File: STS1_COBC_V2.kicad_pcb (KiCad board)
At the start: 4 copper layers, 81 x 85 mm, 82 parts, among them IC2 STWD100PYW83F, IC3 STM32F411RET6TR, J1 Conn_Coaxial, J10 Conn_01x01_Male, J11 Conn_01x01_Male, J12 Conn_01x01_Male, J13 Conn_01x01_Male, J14 Conn_01x01_Male, J15 Conn_01x01_Male, J16 Conn_ARM_JTAG_SWD_10, J17 Conn_01x03_Male, J18 Conn_01x01_Male, J2 Conn_01x03_Male, J3 Conn_01x01_Male, J4 Conn_01x01_Female, J5 Conn_01x03_Male, J9 Conn_01x03_Male, U1 coordinate_system, U3 MCP1725-3302E_MC, Y1 Crystal_GND24

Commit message: more work done
All parts besides RF added
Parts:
- removed D3, D4, D5: LED, LED_SMD:LED_0805_2012Metric
- removed J10, J11, J14, J15, J3: Conn_01x01_Male, Connector_PinHeader_2.54mm:PinHeader_1x01_P2.54mm_Vertical
- removed J4: Conn_01x01_Female, Connector_PinHeader_2.54mm:PinHeader_1x01_P2.54mm_Vertical
- removed J9: Conn_01x03_Male, STS1library:PinHeader_1x03_P2.54mm_Vertical_umdieEcke
- removed R4, R6, R7: 300, Resistor_SMD:R_0805_2012Metric
- removed TP1, TP10, TP11, TP12, TP13, TP14, TP15, TP2, TP3, TP7, TP8, TP9: TestPoint, STS1library:STS1_Testpoint
- added 5V_RF: TestPoint, STS1library:STS1_Testpoint, F.Cu at (180.4, 57.4)
- added C36: 100uF, Capacitor_Tantalum_SMD:CP_EIA-7343-43_Kemet-X, F.Cu at (127.2, 78.8)
- added C37: 22uF, Capacitor_SMD:C_1206_3216Metric, F.Cu at (128.3, 73.1)
- added C38: 100nF, Capacitor_SMD:C_0603_1608Metric, F.Cu at (130.4, 75.8)
- added C39: 1uF, Capacitor_SMD:C_0805_2012Metric, F.Cu at (125.1, 70.3)
- added C40: 1uF, Capacitor_SMD:C_0805_2012Metric, F.Cu at (135.4, 79.5)
- added C41: 22nF, Capacitor_SMD:C_0603_1608Metric, F.Cu at (133.4, 79.3)
- added C42: 100nF, Capacitor_SMD:C_0603_1608Metric, F.Cu at (132.2, 72.7)
- added C43: 100nF, Capacitor_SMD:C_0603_1608Metric, F.Cu at (135.2, 72.7)
- added C44: 100nF, Capacitor_SMD:C_0603_1608Metric, F.Cu at (136.8, 76.2)
- added C45: 10uF, Capacitor_SMD:C_0805_2012Metric, F.Cu at (138.6, 76.5)
- added C46: 10uF, Capacitor_SMD:C_0805_2012Metric, F.Cu at (138.5, 73.7)
- added C47: 100uF, Capacitor_Tantalum_SMD:CP_EIA-7343-43_Kemet-X, F.Cu at (142.0, 79.2)
- added D10: BZY55C12 RYG, Diode_SMD:D_0805_2012Metric, F.Cu at (127.9, 84.2)
- added D11: AQ1003-01LTG, Diode_SMD:D_SOD-523, F.Cu at (140.9, 73.4)
- added D9: UCLAMP0871P.TNT, STS_Package_DFN_QFN:SGP1610N2, F.Cu at (124.0, 75.5)
- added EDU_EN: TestPoint, STS1library:STS1_Testpoint, F.Cu at (169.7, 118.4)
- added FLASH_CLK: Conn_01x01_Male, Connector_PinHeader_2.54mm:PinHeader_1x01_P2.54mm_Vertical, F.Cu at (126.2, 107.9)
- added FLASH_MISO: Conn_01x01_Male, Connector_PinHeader_2.54mm:PinHeader_1x01_P2.54mm_Vertical, F.Cu at (130.1, 112.2)
- added FLASH_MOSI: Conn_01x01_Male, Connector_PinHeader_2.54mm:PinHeader_1x01_P2.54mm_Vertical, F.Cu at (126.2, 112.2)
- added FLASH_VDD: TestPoint, STS1library:STS1_Testpoint, F.Cu at (145.3, 108.0)
- added FRAM_CLK: Conn_01x01_Male, Connector_PinHeader_2.54mm:PinHeader_1x01_P2.54mm_Vertical, F.Cu at (130.1, 99.2)
- added FRAM_CS: TestPoint, STS1library:STS1_Testpoint, F.Cu at (132.8, 109.4)
- added FRAM_MISO: Conn_01x01_Male, Connector_PinHeader_2.54mm:PinHeader_1x01_P2.54mm_Vertical, F.Cu at (130.1, 103.6)
- added FRAM_MOSI: Conn_01x01_Male, Connector_PinHeader_2.54mm:PinHeader_1x01_P2.54mm_Vertical, F.Cu at (130.1, 107.9)
- added FRAM_VDD: TestPoint, STS1library:STS1_Testpoint, F.Cu at (144.3, 100.1)
- added L2: 4.7uH, Inductor_SMD:L_12x12mm_H6mm, F.Cu at (133.8, 65.3)
- added PA12: TestPoint, STS1library:STS1_Testpoint, F.Cu at (185.3, 105.4)
- added PA4: TestPoint, STS1library:STS1_Testpoint, F.Cu at (163.0, 119.3)
- added PB10: TestPoint, STS1library:STS1_Testpoint, F.Cu at (170.7, 116.8)
- added Q2: BSS123, Package_TO_SOT_SMD:SOT-23, F.Cu at (135.9, 83.3)
- added R14: 10k, Resistor_SMD:R_0603_1608Metric, F.Cu at (130.4, 81.9)
- added R15: 1M, Resistor_SMD:R_0603_1608Metric, F.Cu at (133.4, 83.8)
- added R16: 100mR, Resistor_SMD:R_0603_1608Metric, F.Cu at (125.2, 72.8)
- added R17: 100k, Resistor_SMD:R_0603_1608Metric, F.Cu at (130.4, 78.9)
- added R18: 33k, Resistor_SMD:R_0603_1608Metric, F.Cu at (131.9, 79.3)
- added R19: 21k5, Resistor_SMD:R_0603_1608Metric, F.Cu at (132.7, 81.6)
- added STM_VDD: TestPoint, STS1library:STS1_Testpoint, F.Cu at (160.9, 98.5)
- added STM_VDD: TestPoint, STS1library:STS1_Testpoint, F.Cu at (177.0, 101.9)
- added STM_VDD: TestPoint, STS1library:STS1_Testpoint, F.Cu at (163.5, 118.3)
- added STM_VDD: TestPoint, STS1library:STS1_Testpoint, F.Cu at (176.1, 115.2)
- added U6: ~, STS_Package_DFN_QFN:MP28167_QFN16, F.Cu at (133.9, 75.7)
- added WD_VDD: TestPoint, STS1library:STS1_Testpoint, F.Cu at (152.5, 116.5)
- CSBI_1, CSBI_2: value Conn_02x25_Odd_Even -> ~
- J1: footprint Connector_Coaxial:SMA_Amphenol_901-144_Vertical -> Connector_Coaxial:SMB_Jack_Vertical
- moved C13 138.1 mm to (157.3, 101.2), turned to 180 degrees
- moved C11 137.3 mm to (156.0, 115.0), turned to 90 degrees
- moved IC2 135.7 mm to (153.1, 114.7)
- moved Y1 134.7 mm to (152.8, 102.1), turned to 180 degrees
- moved C15 132.9 mm to (156.5, 106.2), turned to -90 degrees
- moved C19 130.5 mm to (163.7, 100.9), turned to 180 degrees
- moved C20 126.6 mm to (163.7, 98.9), turned to 180 degrees
- moved C23 126.5 mm to (177.0, 104.2), turned to -90 degrees
- moved C21 126.0 mm to (172.4, 117.7), turned to -90 degrees
- moved PC1 123.1 mm to (160.6, 119.4)
- moved C14 121.0 mm to (154.0, 106.6), turned to 90 degrees
- moved J16 114.3 mm to (181.7, 121.3)
- moved C16 113.7 mm to (158.0, 111.0), turned to 90 degrees
- moved R3 111.9 mm to (153.0, 112.3)
- moved R5 110.9 mm to (158.7, 104.5), turned to 90 degrees
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- renumbered J12 to PC0, J13 to PC1, J18 to SPI4_NSS
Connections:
- net /COBC RF/RF4463_ANT_GND renamed Net-(J1-Pad2)
- net Net-(CSBI_2-Pad13) renamed /STS1_connector/EPS_BAT_FAULT
- C1 pad 1: /COBC RF/RF4463_VCC -> +5V
- C11 pad 1: /COBC STM/Watchdog_VCC -> +3V3
- C12 pad 1: /COBC STM/Watchdog_VCC -> +3V3
- C2 pad 1: /COBC RF/RF4463_VCC -> +5V
- CSBI_1 pad 1: GND -> AGND
- CSBI_1 pad 10: GND -> AGND
- CSBI_1 pad 2: GND -> AGND
- CSBI_1 pad 23: GND -> AGND
- CSBI_1 pad 24: GND -> AGND
- CSBI_1 pad 25: Net-(CSBI_1-Pad25) -> unconnected-(CSBI_1-Pad25)
- CSBI_1 pad 26: Net-(CSBI_1-Pad25) -> unconnected-(CSBI_1-Pad25)
- CSBI_1 pad 27: Net-(CSBI_1-Pad27) -> unconnected-(CSBI_1-Pad27)
- CSBI_1 pad 28: Net-(CSBI_1-Pad27) -> unconnected-(CSBI_1-Pad27)
- CSBI_1 pad 29: Net-(CSBI_1-Pad29) -> unconnected-(CSBI_1-Pad29)
- CSBI_1 pad 3: GND -> AGND
- CSBI_1 pad 30: Net-(CSBI_1-Pad29) -> unconnected-(CSBI_1-Pad29)
- CSBI_1 pad 31: Net-(CSBI_1-Pad31) -> unconnected-(CSBI_1-Pad31)
- CSBI_1 pad 32: Net-(CSBI_1-Pad31) -> unconnected-(CSBI_1-Pad31)
- CSBI_1 pad 33: GND -> AGND
- CSBI_1 pad 34: GND -> AGND
- CSBI_1 pad 35: /STS1_connector/EDU_Heartbeat -> /EDU_Heartbeat
- CSBI_1 pad 36: /STS1_connector/EDU_Heartbeat -> /EDU_Heartbeat
- CSBI_1 pad 37: /STS1_connector/EDU_UPDATE -> /EDU_Update
- CSBI_1 pad 38: /STS1_connector/EDU_UPDATE -> /EDU_Update
- CSBI_1 pad 39: /STS1_connector/EDU_EN -> /EDU_EN
- CSBI_1 pad 4: GND -> AGND
- CSBI_1 pad 40: /STS1_connector/EDU_EN -> /EDU_EN
- CSBI_1 pad 41: GND -> AGND
- CSBI_1 pad 42: GND -> AGND
- CSBI_1 pad 47: GND -> AGND
- CSBI_1 pad 48: GND -> AGND
- CSBI_1 pad 49: GND -> AGND
- CSBI_1 pad 50: GND -> AGND
- CSBI_1 pad 9: GND -> AGND
- CSBI_2 pad 1: GND -> AGND
- CSBI_2 pad 10: GND -> AGND
- CSBI_2 pad 11: Net-(CSBI_2-Pad11) -> unconnected-(CSBI_2-Pad11)
- CSBI_2 pad 12: Net-(CSBI_2-Pad11) -> unconnected-(CSBI_2-Pad11)
- CSBI_2 pad 15: /STS1_connector/EDU_BOOT -> /EDU_BOOT
- CSBI_2 pad 16: /STS1_connector/EDU_BOOT -> /EDU_BOOT
- CSBI_2 pad 17: GND -> AGND
- CSBI_2 pad 18: GND -> AGND
- CSBI_2 pad 19: /STS1_connector/UCI_COBC_3V3 -> +3V3
- CSBI_2 pad 2: GND -> AGND
- CSBI_2 pad 20: /STS1_connector/UCI_COBC_3V3 -> +3V3
- CSBI_2 pad 21: /STS1_connector/EPS_BAT_GOOD -> /EPS_BAT_GOOD
- CSBI_2 pad 22: /STS1_connector/EPS_BAT_GOOD -> /EPS_BAT_GOOD
- CSBI_2 pad 23: /STS1_connector/EPS_ANT_DEPLOYED -> /EPS_ANT_DEP
- CSBI_2 pad 24: /STS1_connector/EPS_ANT_DEPLOYED -> /EPS_ANT_DEP
- CSBI_2 pad 25: /STS1_connector/EPS_CHARGING -> /EPS_Charging
- CSBI_2 pad 26: /STS1_connector/EPS_CHARGING -> /EPS_Charging
- CSBI_2 pad 27: GND -> AGND
- CSBI_2 pad 28: GND -> AGND
- CSBI_2 pad 3: GND -> AGND
- CSBI_2 pad 4: GND -> AGND
- CSBI_2 pad 41: GND -> AGND
- CSBI_2 pad 42: GND -> AGND
- CSBI_2 pad 47: GND -> AGND
- CSBI_2 pad 48: GND -> AGND
- CSBI_2 pad 49: GND -> AGND
- CSBI_2 pad 50: GND -> AGND
- CSBI_2 pad 9: GND -> AGND
- IC2 pad 3: Net-(IC2-Pad3) -> AGND
- IC2 pad 5: /COBC STM/Watchdog_VCC -> +3V3
- IC3 pad 15: /COBC STM/SPI4_MOSI -> /RF4463_SDI
- IC3 pad 34: /COBC STM/SPI4_CLK -> /RF4463_CLK
- IC3 pad 35: /COBC STM/RF4463F30_SDN -> /RF4463F30_SDN
- IC3 pad 37: /COBC STM/RF4463F30_GPIO_0 -> /RF4463F30_GPIO_0
- IC3 pad 39: /COBC STM/RF4463F30_GPIO_1 -> /RF4463F30_GPIO_1
- IC3 pad 41: /COBC STM/SPI4_CS_RF -> /RF4463_nSEL
- IC3 pad 44: /COBC STM/SPI4_MISO -> /RF4463_SDO
- IC3 pad 51: /STS1_connector/EDU_SPI_1 -> /STS1_connector/COBC_SPI_1
- IC3 pad 52: /STS1_connector/EDU_SPI_3 -> /STS1_connector/COBC_SPI_3
- IC3 pad 53: /STS1_connector/EDU_SPI_2 -> /STS1_connector/COBC_SPI_2
- IC3 pad 54: /STS1_connector/EDU_SPI_4 -> /STS1_connector/COBC_SPI_4
- IC3 pad 56: /STS1_connector/EDU_SPI_5 -> /STS1_connector/COBC_SPI_5
- IC3 pad 57: /STS1_connector/EDU_SPI_6 -> /STS1_connector/COBC_SPI_6
- IC3 pad 58: /COBC STM/RF4463F30_nIRQ -> /RF4463F30_nIRQ
- IC3 pad 59: /COBC STM/EDU_Boot -> /EDU_BOOT
- IC3 pad 61: /COBC STM/PB8 -> /DCDC_nEN
- J2 pad 3: /COBC RF/RF4463F30_GPIO0 -> /RF4463F30_GPIO_0
- RF1 pad 1: /COBC RF/RF4463_VCC -> +5V
- RF1 pad 10: /COBC RF/RF4463_SDI -> /RF4463_SDI
- RF1 pad 11: /COBC RF/RF4463_SDO -> /RF4463_SDO
- RF1 pad 12: /COBC RF/RF4463F30_GPIO1 -> /RF4463F30_GPIO_1
- RF1 pad 5: /COBC RF/RF4463F30_SDN -> /RF4463F30_SDN
- RF1 pad 6: /COBC RF/RF4463_nIRQ -> /RF4463F30_nIRQ
- RF1 pad 7: /COBC RF/RF4463_nSEL -> /RF4463_nSEL
- RF1 pad 9: /COBC RF/RF4463_SPI_CLK -> /RF4463_CLK
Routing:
- net AGND: track 13.1 -> 115.1 mm, vias 0 -> 108
- net /EDU_Update: track 0.00 -> 85.7 mm, vias 0 -> 1
- net /EDU_Heartbeat: track 0.00 -> 84.8 mm
- net +5V: track 0.00 -> 83.2 mm
- net /EDU_EN: track 0.00 -> 68.5 mm, vias 0 -> 1
- net +3V3: track 13.2 -> 75.8 mm, vias 0 -> 14
- net /RF4463F30_GPIO_0: track 0.00 -> 62.0 mm, vias 0 -> 2
- net /RF4463_SDO: track 0.00 -> 57.4 mm, vias 0 -> 2
- net /DCDC_nEN: track 0.00 -> 55.6 mm, vias 0 -> 2
- net /RF4463F30_SDN: track 0.00 -> 54.2 mm, vias 0 -> 2
- net /RF4463F30_GPIO_1: track 0.00 -> 54.1 mm
- net /EPS_BAT_GOOD: track 0.00 -> 51.7 mm, vias 0 -> 2
- net /COBC STM/STM32_NRST: track 0.00 -> 49.8 mm, vias 0 -> 4
- net /RF4463_nSEL: track 0.00 -> 48.6 mm, vias 0 -> 2
- net GND: track 48.0 -> 0.00 mm
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- added copper zone on B.Cu, net +3V3
- added copper zone on F.Cu, net +5V
- added copper zone on F.Cu, net AGND
- added copper zone on F.Cu, net Net-(C42-Pad1)
- added copper zone on F.Cu, net Net-(C43-Pad1)
- added copper zone on F.Cu, net VBUS
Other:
- board text added: "TU Wien Space Team STS [COBC] [V2]"
- board text removed: "TU Wien Space Team STS [PCB name] [Version]"

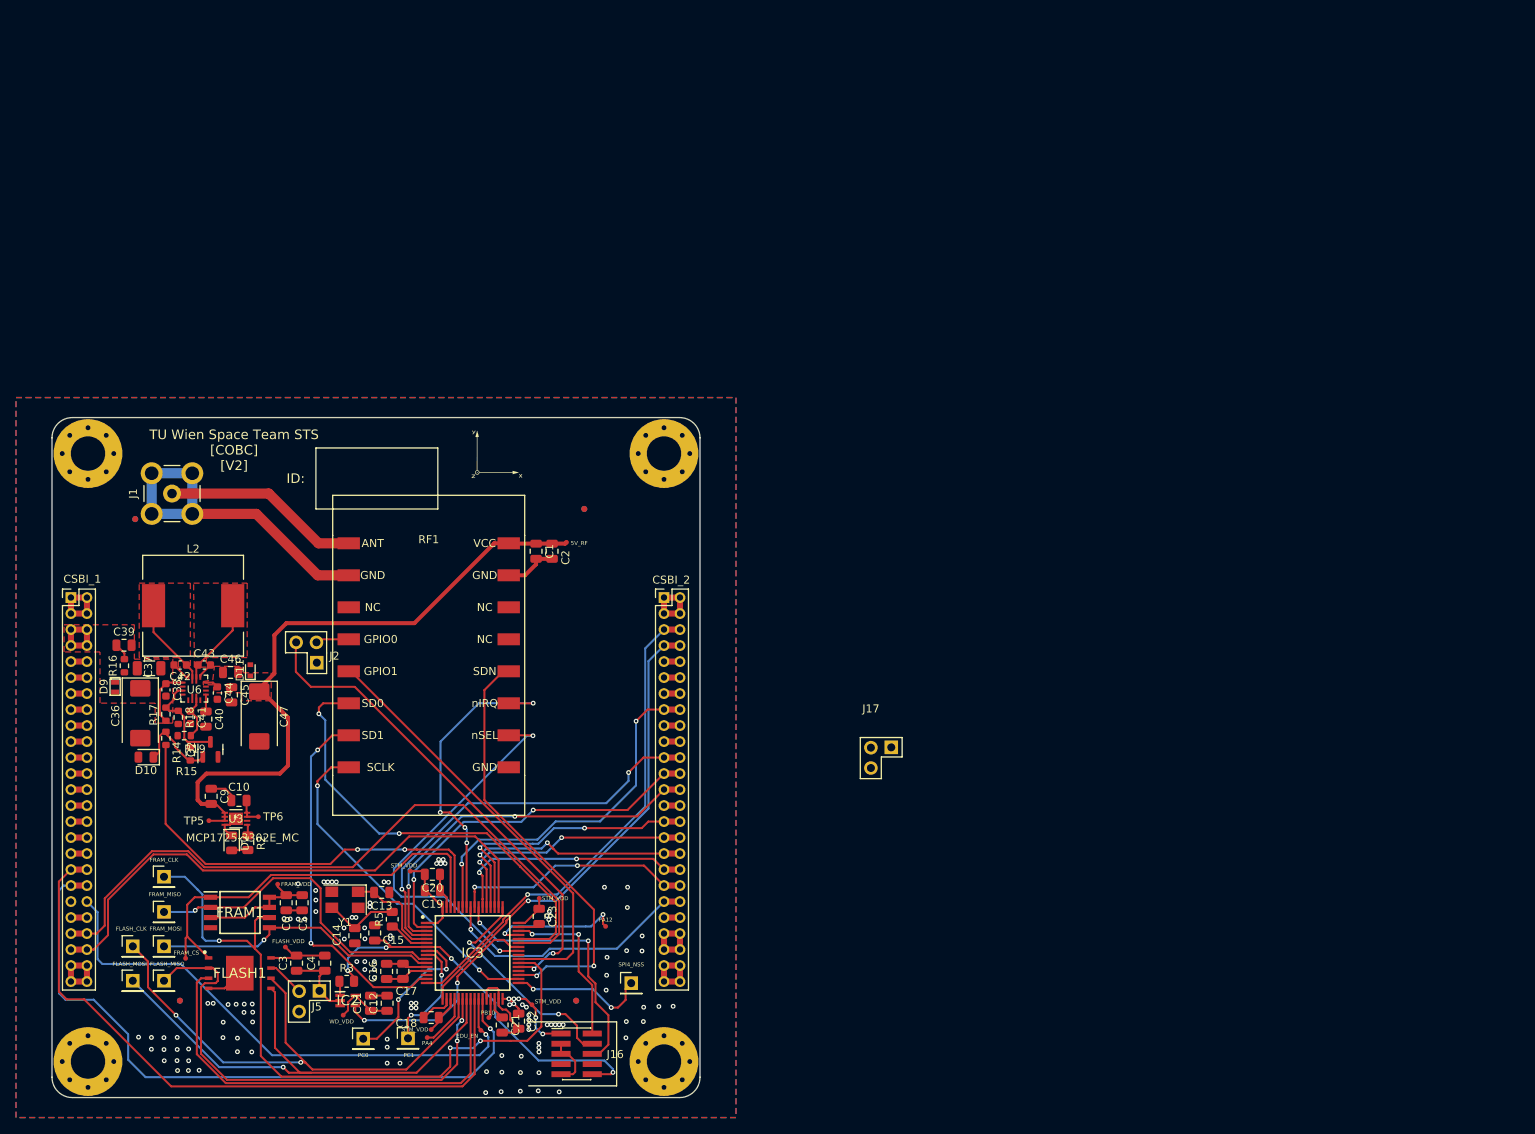
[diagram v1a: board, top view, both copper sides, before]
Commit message: add RF part
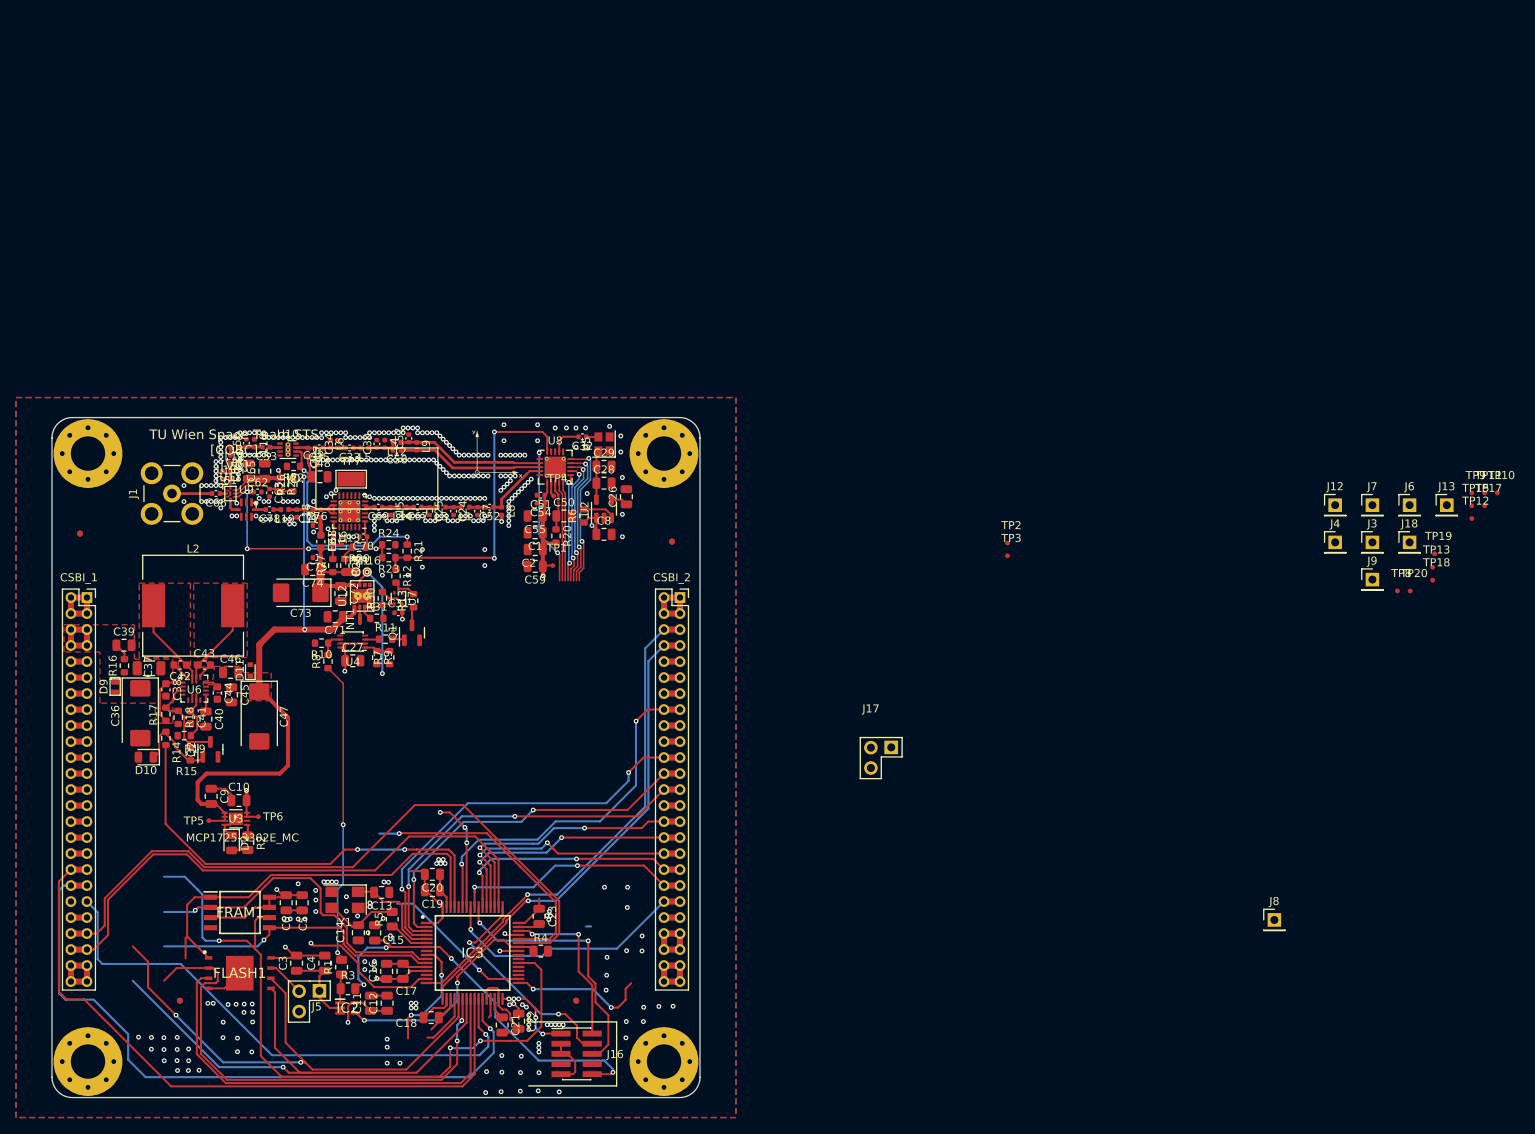
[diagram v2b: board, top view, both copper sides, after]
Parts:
- removed 5V_RF, EDU_EN, FLASH_VDD, FRAM_CS, FRAM_VDD, PA12, PA4, PB10, STM_VDD (x4), WD_VDD: TestPoint, STS1library:STS1_Testpoint
- removed FLASH_CLK, FLASH_MISO, FLASH_MOSI, FRAM_CLK, FRAM_MISO, FRAM_MOSI, PC0, PC1, SPI4_NSS: Conn_01x01_Male, Connector_PinHeader_2.54mm:PinHeader_1x01_P2.54mm_Vertical
- removed J2: Conn_01x03_Male, STS1library:PinHeader_1x03_P2.54mm_Vertical_umdieEcke
- removed RF1: RF4463F30, STS1_RF:STS1_RF4463F30
- added C24: 12p, Capacitor_SMD:C_0402_1005Metric, F.Cu at (166.3, 53.5)
- added C25: 18p, Capacitor_SMD:C_0402_1005Metric, F.Cu at (163.3, 53.5)
- added C26: 10n, Capacitor_SMD:C_0805_2012Metric, F.Cu at (187.9, 51.7)
- added C27: 100n, Capacitor_SMD:C_0805_2012Metric, F.Cu at (153.7, 72.2)
- added C28: 4.7µ, Capacitor_SMD:C_0805_2012Metric, F.Cu at (185.1, 50.0)
- added C29: 100n, Capacitor_SMD:C_0805_2012Metric, F.Cu at (185.1, 47.9)
- added C30: 24p, Capacitor_SMD:C_0402_1005Metric, F.Cu at (156.7, 45.1)
- added C31: 100p, Capacitor_SMD:C_0402_1005Metric, F.Cu at (159.4, 66.2)
- added C32: 100p, Capacitor_SMD:C_0402_1005Metric, F.Cu at (182.4, 44.2)
- added C33: 2p, Capacitor_SMD:C_0402_1005Metric, F.Cu at (153.3, 45.6)
- added C34: 24p, Capacitor_SMD:C_0402_1005Metric, F.Cu at (151.9, 45.1)
- added C35: 100p, Capacitor_SMD:C_0402_1005Metric, F.Cu at (149.5, 45.6)
- added C48: 1u, Capacitor_SMD:C_0805_2012Metric, F.Cu at (149.6, 49.2)
- added C49: 100p, Capacitor_SMD:C_0402_1005Metric, F.Cu at (148.8, 47.7)
- added C50: 100n, Capacitor_SMD:C_0805_2012Metric, F.Cu at (180.1, 54.1)
- added C51: 33p, Capacitor_SMD:C_0402_1005Metric, F.Cu at (177.2, 51.5)
- added C52: C, Capacitor_SMD:C_0402_1005Metric, F.Cu at (170.8, 53.0)
- added C53: 100p, Capacitor_SMD:C_0402_1005Metric, F.Cu at (142.9, 45.5)
- added C54: 100p, Capacitor_SMD:C_0402_1005Metric, F.Cu at (177.2, 52.5)
- added C55: 10n, Capacitor_SMD:C_0805_2012Metric, F.Cu at (176.5, 54.1)
- added C56: 24p, Capacitor_SMD:C_0402_1005Metric, F.Cu at (140.4, 45.0)
- added C57: C, Capacitor_SMD:C_0402_1005Metric, F.Cu at (160.7, 44.4)
- added C58: C, Capacitor_SMD:C_0402_1005Metric, F.Cu at (159.2, 45.9)
- added C59: 47µ, Capacitor_SMD:C_0805_2012Metric, F.Cu at (176.5, 60.4)
- added C60: 2p, Capacitor_SMD:C_0402_1005Metric, F.Cu at (138.4, 47.0)
- added C61: 24p, Capacitor_SMD:C_0402_1005Metric, F.Cu at (137.9, 48.5)
- added C62: 100p, Capacitor_SMD:C_0402_1005Metric, F.Cu at (141.8, 51.1)
- added C63: 100p, Capacitor_SMD:C_0402_1005Metric, F.Cu at (143.3, 51.2)
- added C64: 100n, Capacitor_SMD:C_0805_2012Metric, F.Cu at (140.7, 48.5)
- added C65: 1µ, Capacitor_SMD:C_0805_2012Metric, F.Cu at (142.7, 48.5)
- added C66: 100p, Capacitor_SMD:C_0402_1005Metric, F.Cu at (136.6, 51.3)
- added C67: 2p, Capacitor_SMD:C_0402_1005Metric, F.Cu at (161.8, 53.0)
- added C68: 100n, Capacitor_SMD:C_0402_1005Metric, F.Cu at (152.3, 57.2)
- added C69: 62p, Capacitor_SMD:C_0402_1005Metric, F.Cu at (156.9, 53.0)
- added C7: 18p, Capacitor_SMD:C_0402_1005Metric, F.Cu at (169.3, 53.5)
- added C70: 100p, Capacitor_SMD:C_0402_1005Metric, F.Cu at (155.0, 56.7)
- added C71: 10u, Capacitor_SMD:C_0805_2012Metric, F.Cu at (151.5, 66.7)
- added C72: 100n, Capacitor_SMD:C_0805_2012Metric, F.Cu at (152.2, 63.8)
- added C73: 10u, Capacitor_Tantalum_SMD:CP_EIA-6032-28_Kemet-C, F.Cu at (147.2, 63.7)
- added C74: 1n, Capacitor_SMD:C_0805_2012Metric, F.Cu at (148.7, 60.8)
- added C75: 100p, Capacitor_SMD:C_0402_1005Metric, F.Cu at (149.2, 59.3)
- added C76: 100p, Capacitor_SMD:C_0402_1005Metric, F.Cu at (149.2, 55.3)
- added C77: 24p, Capacitor_SMD:C_0402_1005Metric, F.Cu at (148.2, 53.3)
- added C78: 3.3p, Capacitor_SMD:C_0402_1005Metric, F.Cu at (143.3, 53.3)
- added C8: 100n, Capacitor_SMD:C_0805_2012Metric, F.Cu at (185.1, 56.4)
- added FB1: Ferrite_Bead, Inductor_SMD:L_0603_1608Metric, F.Cu at (149.7, 57.3)
- added J12: Conn_01x01_Male, Connector_PinHeader_2.54mm:PinHeader_1x01_P2.54mm_Vertical, F.Cu at (276.5, 52.8)
- added J13: Conn_01x01_Male, Connector_PinHeader_2.54mm:PinHeader_1x01_P2.54mm_Vertical, F.Cu at (290.5, 52.8)
- added J18: Conn_01x01_Male, Connector_PinHeader_2.54mm:PinHeader_1x01_P2.54mm_Vertical, F.Cu at (285.8, 57.4)
- added J3: Conn_01x01_Male, Connector_PinHeader_2.54mm:PinHeader_1x01_P2.54mm_Vertical, F.Cu at (281.2, 57.4)
- added J4: Conn_01x01_Male, Connector_PinHeader_2.54mm:PinHeader_1x01_P2.54mm_Vertical, F.Cu at (276.5, 57.4)
- added J6: Conn_01x01_Male, Connector_PinHeader_2.54mm:PinHeader_1x01_P2.54mm_Vertical, F.Cu at (285.8, 52.8)
- added J7: Conn_01x01_Male, Connector_PinHeader_2.54mm:PinHeader_1x01_P2.54mm_Vertical, F.Cu at (281.2, 52.8)
- added J8: Conn_01x01_Male, Connector_PinHeader_2.54mm:PinHeader_1x01_P2.54mm_Vertical, F.Cu at (268.9, 104.6)
- added J9: Conn_01x01_Male, Connector_PinHeader_2.54mm:PinHeader_1x01_P2.54mm_Vertical, F.Cu at (281.2, 62.0)
- added L1: 15n, Inductor_SMD:L_0402_1005Metric, F.Cu at (167.8, 53.0)
- added L10: 5.6n, Inductor_SMD:L_0402_1005Metric, F.Cu at (141.4, 45.0)
- added L11: 68n, Inductor_SMD:L_0402_1005Metric, F.Cu at (138.9, 45.5)
- added L12: L, Inductor_SMD:L_0402_1005Metric, F.Cu at (159.2, 44.9)
- added L13: 5.6n, Inductor_SMD:L_0402_1005Metric, F.Cu at (137.9, 49.5)
- added L14: 68n, Inductor_SMD:L_0402_1005Metric, F.Cu at (159.9, 53.0)
- added L15: 3.2n, Inductor_SMD:L_0402_1005Metric, F.Cu at (158.4, 53.5)
- added L16: 68n, Inductor_SMD:L_0402_1005Metric, F.Cu at (151.3, 57.2)
- added L17: 18n, Inductor_SMD:L_0402_1005Metric, F.Cu at (149.7, 53.8)
- added L18: 8.2n, Inductor_SMD:L_0402_1005Metric, F.Cu at (146.7, 53.8)
- added L19: 47n, Inductor_SMD:L_0402_1005Metric, F.Cu at (145.2, 53.3)
- added L3: 15n, Inductor_SMD:L_0402_1005Metric, F.Cu at (164.8, 53.0)
- added L4: 5.6n, Inductor_SMD:L_0402_1005Metric, F.Cu at (157.7, 45.1)
- added L5: 68n, Inductor_SMD:L_0402_1005Metric, F.Cu at (155.2, 45.6)
- added L6: 5.6n, Inductor_SMD:L_0402_1005Metric, F.Cu at (150.9, 45.1)
- added L7: 68n, Inductor_SMD:L_0402_1005Metric, F.Cu at (148.1, 46.1)
- added L8: L, Inductor_SMD:L_0402_1005Metric, F.Cu at (172.3, 53.5)
- added L9: L, Inductor_SMD:L_0402_1005Metric, F.Cu at (161.7, 45.4)
- added NT1: Net-Tie_2, NetTie:NetTie-2_SMD_Pad0.5mm, F.Cu at (154.6, 67.0)
- added Q1: SQ2318, Package_TO_SOT_SMD:SOT-23, F.Cu at (161.1, 68.7)
- added R1: 4k7, Resistor_SMD:R_0805_2012Metric, F.Cu at (152.3, 110.5)
- added R10: 10k, Resistor_SMD:R_0603_1608Metric, F.Cu at (149.8, 70.0)
- added R11: 100, Resistor_SMD:R_0603_1608Metric, F.Cu at (157.8, 69.5)
- added R12: 10k, Resistor_SMD:R_0603_1608Metric, F.Cu at (159.1, 61.6)
- added R13: 100, Resistor_SMD:R_0603_1608Metric, F.Cu at (161.3, 64.7)
- added R20: 4.7, Resistor_SMD:R_0603_1608Metric, F.Cu at (179.1, 56.6)
- added R21: 33k, Resistor_SMD:R_0603_1608Metric, F.Cu at (160.5, 58.5)
- added R22: 10k, Resistor_SMD:R_0603_1608Metric, F.Cu at (146.3, 47.9)
- added R23: 5.6k, Resistor_SMD:R_0603_1608Metric, F.Cu at (158.2, 59.3)
- added R24: 6.8k, Resistor_SMD:R_0603_1608Metric, F.Cu at (158.2, 57.7)
- added R25: 5.6k, Resistor_SMD:R_0603_1608Metric, F.Cu at (144.6, 50.2)
- added R26: 6.8k, Resistor_SMD:R_0603_1608Metric, F.Cu at (146.2, 50.2)
- added R27: 240, Resistor_SMD:R_0603_1608Metric, F.Cu at (151.2, 60.3)
- added R28: 280, Resistor_SMD:R_0603_1608Metric, F.Cu at (152.7, 60.3)
- added R29: 0, Resistor_SMD:R_0603_1608Metric, F.Cu at (154.5, 58.0)
- added R30: 100k, Resistor_SMD:R_0603_1608Metric, F.Cu at (157.4, 64.4)
- added R31: 110k, Resistor_SMD:R_0603_1608Metric, F.Cu at (156.7, 66.9)
- added R4: 4k7, Resistor_SMD:R_0805_2012Metric, F.Cu at (177.2, 108.5)
- added R6: 100k, Resistor_SMD:R_0603_1608Metric, F.Cu at (182.6, 54.1)
- added R7: 100, Resistor_SMD:R_0603_1608Metric, F.Cu at (158.3, 71.8)
- added R8: 100, Resistor_SMD:R_0603_1608Metric, F.Cu at (150.6, 72.3)
- added R9: 10k, Resistor_SMD:R_0603_1608Metric, F.Cu at (156.7, 71.8)
- added TP1: SiVCC, STS1library:STS1_Testpoint, F.Cu at (178.7, 60.3)
- added TP10: TestPoint, STS1library:STS1_Testpoint, F.Cu at (296.8, 51.2)
- added TP11: TestPoint, STS1library:STS1_Testpoint, F.Cu at (295.2, 51.2)
- added TP12: TestPoint, STS1library:STS1_Testpoint, F.Cu at (293.6, 54.4)
- added TP13: TestPoint, STS1library:STS1_Testpoint, F.Cu at (288.7, 60.5)
- added TP15: TestPoint, STS1library:STS1_Testpoint, F.Cu at (293.6, 52.8)
- added TP16: PA_FAULT, lsf-kicad-lib:TestPoint_D0.8mm_Mask-Only, F.Cu at (155.5, 61.1)
- added TP17: TestPoint, STS1library:STS1_Testpoint, F.Cu at (295.2, 52.8)
- added TP18: TestPoint, STS1library:STS1_Testpoint, F.Cu at (288.7, 62.1)
- added TP19: TestPoint, STS1library:STS1_Testpoint, F.Cu at (289.0, 58.8)
- added TP2: TestPoint, STS1library:STS1_Testpoint, F.Cu at (235.6, 57.5)
- added TP20: TestPoint, STS1library:STS1_Testpoint, F.Cu at (285.9, 63.5)
- added TP21: 5V_PA, lsf-kicad-lib:TestPoint_D0.8mm_Mask-Only, F.Cu at (154.1, 61.1)
- added TP3: TestPoint, STS1library:STS1_Testpoint, F.Cu at (235.6, 59.1)
- added TP4: TXRAMP, STS1library:STS1_Testpoint, F.Cu at (178.8, 51.6)
- added TP7: TestPoint, TestPoint:TestPoint_Keystone_5015_Micro-Minature, F.Cu at (153.5, 49.5)
- added TP8: TestPoint, STS1library:STS1_Testpoint, F.Cu at (284.3, 63.5)
- added TP9: TestPoint, STS1library:STS1_Testpoint, F.Cu at (293.6, 51.2)
- added U10: TQP3M9036, lsf-kicad-lib:DFN-8-1EP_2x2mm_P0.5mm_EP0.7x1.6mm_ThermalVias, F.Cu at (145.6, 45.8)
- added U11: QPC1022, STS_Package_LGA:Qorvo_9Pin_1.1x1.5mm_LGA, F.Cu at (138.4, 51.3)
- added U12: FPF2701, lsf-kicad-lib:MLP-8, F.Cu at (154.9, 64.1)
- added U13: TQP7M9106, Package_DFN_QFN:QFN-24-1EP_4x4mm_P0.5mm_EP2.7x2.7mm_ThermalVias, F.Cu at (153.3, 53.5)
- added U2: LP2985-1.8, Package_TO_SOT_SMD:SOT-23-5, F.Cu at (185.1, 53.2)
- added U4: 74LVC2G74, Package_SO:VSSOP-8_2.4x2.1mm_P0.5mm, F.Cu at (153.7, 69.8)
- added U5: TYKTBCSANF-26.000000, Crystal:Crystal_SMD_2520-4Pin_2.5x2.0mm, F.Cu at (185.1, 45.1)
- added U7: NL17SV04XV5T2G, Package_TO_SOT_SMD:SOT-553, F.Cu at (159.4, 64.4)
- added U8: Si4463, Package_DFN_QFN:QFN-20-1EP_4x4mm_P0.5mm_EP2.6x2.6mm_ThermalVias, F.Cu at (179.0, 48.0)
- added U9: LFCG-490+, lsf-kicad-lib:GE0805C-2, F.Cu at (140.4, 53.3)
- C2: value 47u -> 4.7µ
- CSBI_1, CSBI_2: footprint Connector_PinHeader_2.00mm:PinHeader_2x25_P2.00mm_Vertical -> Connector_PinSocket_2.00mm:PinSocket_2x25_P2.00mm_Vertical
- J1: value Conn_Coaxial -> UHF
- moved FID2 11.7 mm to (193.6, 57.3)
- moved FID6 11.7 mm to (193.6, 57.3)
- moved FID3 7.13 mm to (119.6, 56.3)
- moved FID7 7.13 mm to (119.6, 56.3)
- moved C1 2.31 mm to (176.5, 56.2), turned to 180 degrees
- moved C2 2.12 mm to (176.5, 58.3), turned to 180 degrees
- moved CSBI_1 2.00 mm to (120.5, 64.3)
- moved CSBI_2 2.00 mm to (194.6, 64.3)
- moved R3 0.94 mm to (153.1, 113.2)
- moved IC2 0.93 mm to (153.1, 115.6)
- moved C14 0.59 mm to (154.4, 106.2)
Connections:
- C1 pad 1: +5V -> +3V3
- C2 pad 1: +5V -> +3V3
- IC3 pad 15: /RF4463_SDI -> /Si4463_SDI
- IC3 pad 34: /RF4463_CLK -> /Si4463_CLK
- IC3 pad 35: /RF4463F30_SDN -> /Si4463_SDN
- IC3 pad 37: /RF4463F30_GPIO_0 -> /Si4463_GPIO_0
- IC3 pad 39: /RF4463F30_GPIO_1 -> /Si4463_GPIO_1
- IC3 pad 40: /COBC STM/SPI4_CS_LoRa -> unconnected-(IC3-Pad40)
- IC3 pad 41: /RF4463_nSEL -> /Si4463_nSEL
- IC3 pad 44: /RF4463_SDO -> /Si4463_SDO
- IC3 pad 45: Net-(IC3-Pad45) -> /PA_FAULT
- IC3 pad 58: /RF4463F30_nIRQ -> /Si4463_nIRQ
- J1 pad 2: Net-(J1-Pad2) -> AGND
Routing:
- net /RF4463F30_GPIO_0: track 62.0 -> 0.00 mm, vias 2 -> 0
- net /RF4463_SDO: track 57.4 -> 0.00 mm, vias 2 -> 0
- net /RF4463F30_SDN: track 54.2 -> 0.00 mm, vias 2 -> 0
- net /RF4463F30_GPIO_1: track 54.1 -> 0.00 mm
- net /Si4463_SDO: track 0.00 -> 50.9 mm, vias 0 -> 3
- net /RF4463_nSEL: track 48.6 -> 0.00 mm, vias 2 -> 0
- net /RF4463_SDI: track 46.3 -> 0.00 mm, vias 2 -> 0
- net /RF4463_CLK: track 43.1 -> 0.00 mm, vias 2 -> 0
- net Net-(J1-Pad2): track 43.1 -> 0.00 mm
- net +3V3: track 75.8 -> 118.3 mm, vias 14 -> 25
- net /RF4463F30_nIRQ: track 39.4 -> 0.00 mm, vias 4 -> 0
- net /COBC_old_RF/TX_Active: track 0.00 -> 38.4 mm, vias 0 -> 2
- net /~{WDT_TRIG}: track 0.00 -> 37.7 mm, vias 0 -> 2
- net /Si4463_SDI: track 0.00 -> 35.3 mm, vias 0 -> 3
- net /Si4463_CLK: track 0.00 -> 34.3 mm, vias 0 -> 3
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
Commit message: ordered version cobc v2
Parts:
- removed J18: Conn_01x01_Male, Connector_PinHeader_2.54mm:PinHeader_1x01_P2.54mm_Vertical
- removed TP18, TP19, TP20: TestPoint, STS1library:STS1_Testpoint
- moved TP10 174.0 mm to (132.8, 109.4)
- moved J7 164.5 mm to (126.2, 108.0)
- moved J6 163.7 mm to (130.2, 103.6)
- moved J9 162.9 mm to (126.2, 112.2)
- moved J3 159.2 mm to (130.2, 108.0)
- moved J4 152.2 mm to (130.2, 99.3)
- moved TP11 148.8 mm to (162.9, 119.3)
- moved TP17 147.2 mm to (163.4, 118.3)
- moved J13 146.1 mm to (160.5, 119.6)
- moved TP9 140.9 mm to (160.8, 98.5)
- moved J8 138.9 mm to (130.2, 112.2)
- moved J12 138.6 mm to (155.1, 119.6)
- moved TP12 137.9 mm to (170.6, 116.9)
- moved TP8 135.4 mm to (159.5, 116.0)
- moved TP15 126.4 mm to (177.0, 101.8)
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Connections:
- CSBI_2 pad 13: /STS1_connector/EPS_BAT_FAULT -> /EPS_BAT_FAULT
- CSBI_2 pad 14: /STS1_connector/EPS_BAT_FAULT -> /EPS_BAT_FAULT
- IC3 pad 33: /COBC STM/SPI4_NSS -> unconnected-(IC3-Pad33)
- IC3 pad 9: /COBC STM/PC1 -> /EPS_BAT_FAULT
- J13 pad 1: /COBC STM/PC1 -> /EPS_BAT_FAULT
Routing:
- net VBUS: track 23.4 -> 168.4 mm, vias 0 -> 3
- net /EPS_BAT_FAULT: track 0.00 -> 107.0 mm, vias 0 -> 4
- net /Si4463_SDI: track 35.3 -> 103.7 mm, vias 3 -> 4
- net /Si4463_nSEL: track 21.1 -> 89.1 mm, vias 3 -> 4
- net /Si4463_SDN: track 17.9 -> 81.3 mm, vias 2 -> 4
- net /Si4463_GPIO_0: track 12.4 -> 75.4 mm, vias 0 -> 2
- net /Si4463_GPIO_1: track 12.4 -> 71.6 mm, vias 0 -> 2
- net /WDT_CLR: track 0.00 -> 50.4 mm
- net /Si4463_CLK: track 34.3 -> 84.1 mm, vias 3 -> 4
- net /PA_FAULT: track 18.0 -> 67.2 mm, vias 3 -> 4
- net /Si4463_nIRQ: track 27.4 -> 65.2 mm, vias 5 -> 6
- net /Si4463_SDO: track 50.9 -> 79.3 mm, vias 3 -> 4
- net /COBC STM/PC0: track 0.00 -> 27.2 mm, vias 0 -> 1
- net Net-(IC3-Pad60): track 0.00 -> 20.5 mm, vias 0 -> 1
- net /COBC STM/SPI4_NSS: track 17.4 -> 0.00 mm, vias 2 -> 0
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- removed copper zone on F.Cu, net +5V
- removed copper zone on F.Cu, net Net-(C42-Pad1)
- removed copper zone on F.Cu, net Net-(C43-Pad1)
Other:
- board text added: "Boot_Config"
- board text added: "FL_CLK"
- board text added: "FL_MISO"
- board text added: "FL_MOSI"
- board text added: "FL_VDD"
- board text added: "FR_CLK"
- board text added: "FR_CS"
- board text added: "FR_MISO"
- board text added: "FR_MOSI"
- board text added: "FR_VCC"
- board text added: "PA4"
- board text added: "PB10"
- board text added: "PC0"
- board text added: "PC1"
- board text added: "VCC"
- board text added: "WD_VCC"
